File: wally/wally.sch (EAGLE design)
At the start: 103 parts, among them IC1 ESP32-S3-WROOM-1U-N16, IC2 XTLV61048DBVR, IC3 TLV1117LV33DCYR, IC4 DPS310XTSA1, IC5 BMI323, IC6 MCP96L00T-E_MX, IC7 MLX90395KLW-BBA-001-SP, J1 MSD-4-A, J2 QWIIC_RIGHT_ANGLE, J3 QWIIC_RIGHT_ANGLE, J4 S2B-PH-K-S(LF)(SN), J5 USB4105-GF-A, U1 RA-01H

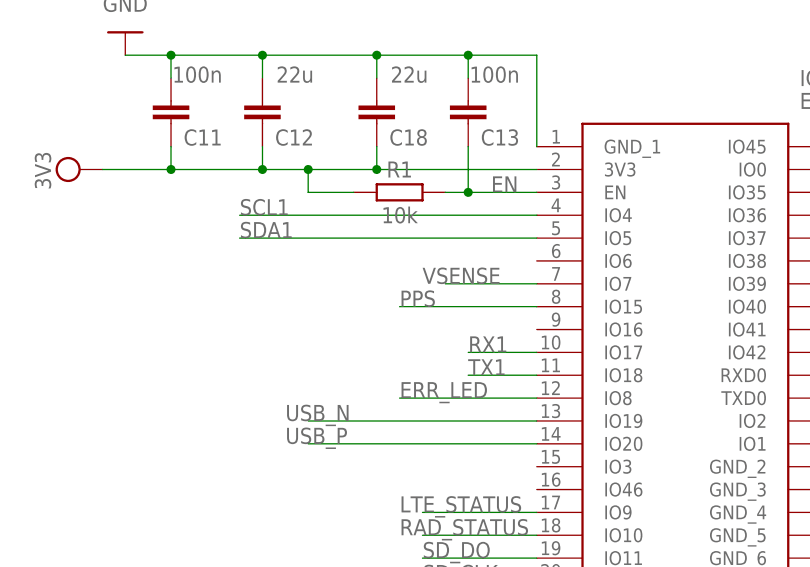
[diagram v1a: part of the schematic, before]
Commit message: add two generic inputs to wally
had two gpio left lol
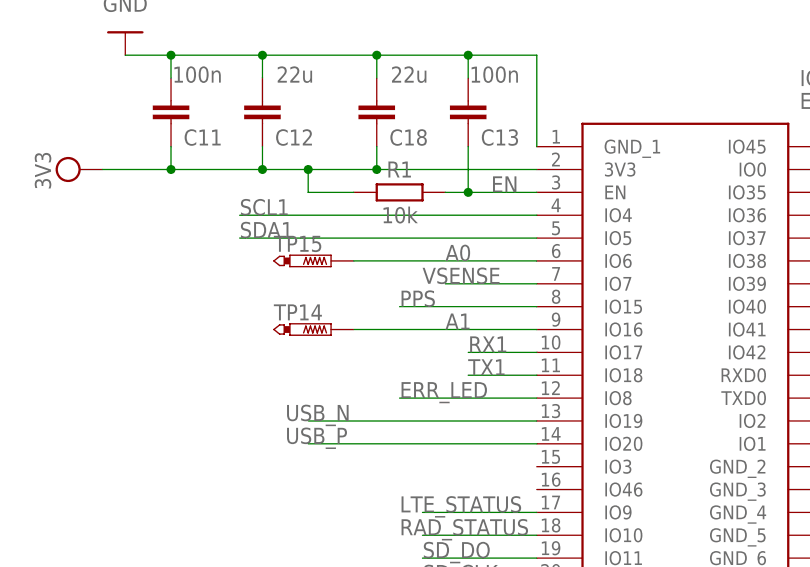
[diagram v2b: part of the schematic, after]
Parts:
- added TP14, TP15: PTR1B2,54, testpad:PTR1B2,54
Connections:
- new net A0: IC1.IO6, TP15.TP
- new net A1: IC1.IO16, TP14.TP
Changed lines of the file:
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@@
 <part name="S1" library="SamacSys_Parts" deviceset="TS-1187A-B-A-B" device="" override_package3d_urn="urn:adsk.eagle:package:44332511/2" override_package_urn="urn:adsk.eagle:footprint:44332512/1"/>
 <part name="S2" library="SamacSys_Parts" deviceset="TS-1187A-B-A-B" device="" override_package3d_urn="urn:adsk.eagle:package:44332514/2" override_package_urn="urn:adsk.eagle:footprint:44332515/1"/>
+<part name="TP14" library="testpad" library_urn="urn:adsk.eagle:library:385" deviceset="PTR1" device="B2,54" package3d_urn="urn:adsk.eagle:package:27948/1"/>
+<part name="TP15" library="testpad" library_urn="urn:adsk.eagle:library:385" deviceset="PTR1" device="B2,54" package3d_urn="urn:adsk.eagle:package:27948/1"/>
 </parts>
 <sheets>
@@
 <attribute name="NAME" x="-130.81" y="15.24" size="1.778" layer="95" align="center-left"/>
 <attribute name="VALUE" x="-130.81" y="12.7" size="1.778" layer="96" align="center-left"/>
+</instance>
+<instance part="TP14" gate="G$1" x="-27.94" y="-22.86" smashed="yes" rot="R270">
+<attribute name="NAME" x="-34.29" y="-21.844" size="1.778" layer="95"/>
+<attribute name="TP_SIGNAL_NAME" x="-30.48" y="-24.13" size="1.778" layer="97" rot="R270"/>
+</instance>
+<instance part="TP15" gate="G$1" x="-27.94" y="-15.24" smashed="yes" rot="R270">
+<attribute name="NAME" x="-34.29" y="-14.224" size="1.778" layer="95"/>
+<attribute name="TP_SIGNAL_NAME" x="-30.48" y="-16.51" size="1.778" layer="97" rot="R270"/>
 </instance>
 </instances>
@@
 </segment>
 </net>
+<net name="A0" class="0">
+<segment>
+<pinref part="IC1" gate="G$1" pin="IO6"/>
+<label x="-15.24" y="-15.24" size="1.778" layer="95"/>
+<pinref part="TP15" gate="G$1" pin="TP"/>
+<wire x1="-25.4" y1="-15.24" x2="-5.08" y2="-15.24" width="0.1524" layer="91"/>
+</segment>
+</net>
+<net name="A1" class="0">
+<segment>
+<pinref part="IC1" gate="G$1" pin="IO16"/>
+<label x="-15.24" y="-22.86" size="1.778" layer="95"/>
+<pinref part="TP14" gate="G$1" pin="TP"/>
+<wire x1="-25.4" y1="-22.86" x2="-5.08" y2="-22.86" width="0.1524" layer="91"/>
+</segment>
+</net>

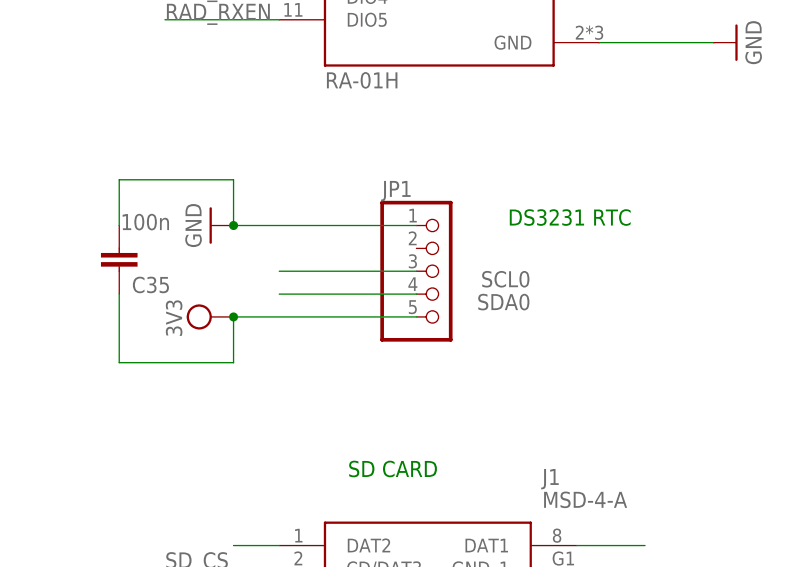
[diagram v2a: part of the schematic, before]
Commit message: move rtc to separate i2c bus
allows all sensors to run at high speed
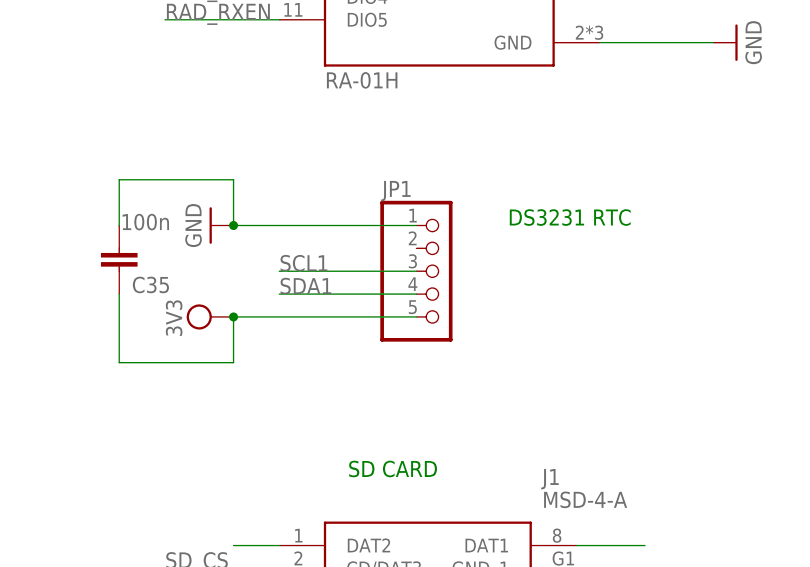
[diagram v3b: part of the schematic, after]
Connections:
- net SCL0: no longer JP1.3
- net SCL1: now also JP1.3
- net SDA0: no longer JP1.4
- net SDA1: now also JP1.4
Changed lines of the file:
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@@
 <net name="SDA0" class="0">
-<segment>
-<pinref part="JP1" gate="A" pin="4"/>
-<wire x1="10.16" y1="-154.94" x2="-5.08" y2="-154.94" width="0.1524" layer="91"/>
-<label x="22.86" y="-154.94" size="1.778" layer="95" rot="R180"/>
-</segment>
 <segment>
 <pinref part="J2" gate="J1" pin="3"/>
@@
 </segment>
 <segment>
-<pinref part="JP1" gate="A" pin="3"/>
-<wire x1="10.16" y1="-152.4" x2="-5.08" y2="-152.4" width="0.1524" layer="91"/>
-<label x="22.86" y="-152.4" size="1.778" layer="95" rot="R180"/>
-</segment>
-<segment>
 <pinref part="R6" gate="G$1" pin="2"/>
 <wire x1="86.36" y1="-30.48" x2="86.36" y2="-38.1" width="0.1524" layer="91"/>
@@
 <label x="-38.1" y="-10.16" size="1.778" layer="95"/>
 </segment>
+<segment>
+<pinref part="JP1" gate="A" pin="3"/>
+<wire x1="10.16" y1="-152.4" x2="-5.08" y2="-152.4" width="0.1524" layer="91"/>
+<label x="-5.08" y="-152.4" size="1.778" layer="95"/>
+</segment>
 </net>
 <net name="SDA1" class="0">
@@
 <label x="-38.1" y="-12.7" size="1.778" layer="95"/>
 </segment>
+<segment>
+<pinref part="JP1" gate="A" pin="4"/>
+<wire x1="10.16" y1="-154.94" x2="-5.08" y2="-154.94" width="0.1524" layer="91"/>
+<label x="-5.08" y="-154.94" size="1.778" layer="95"/>
+</segment>
 </net>

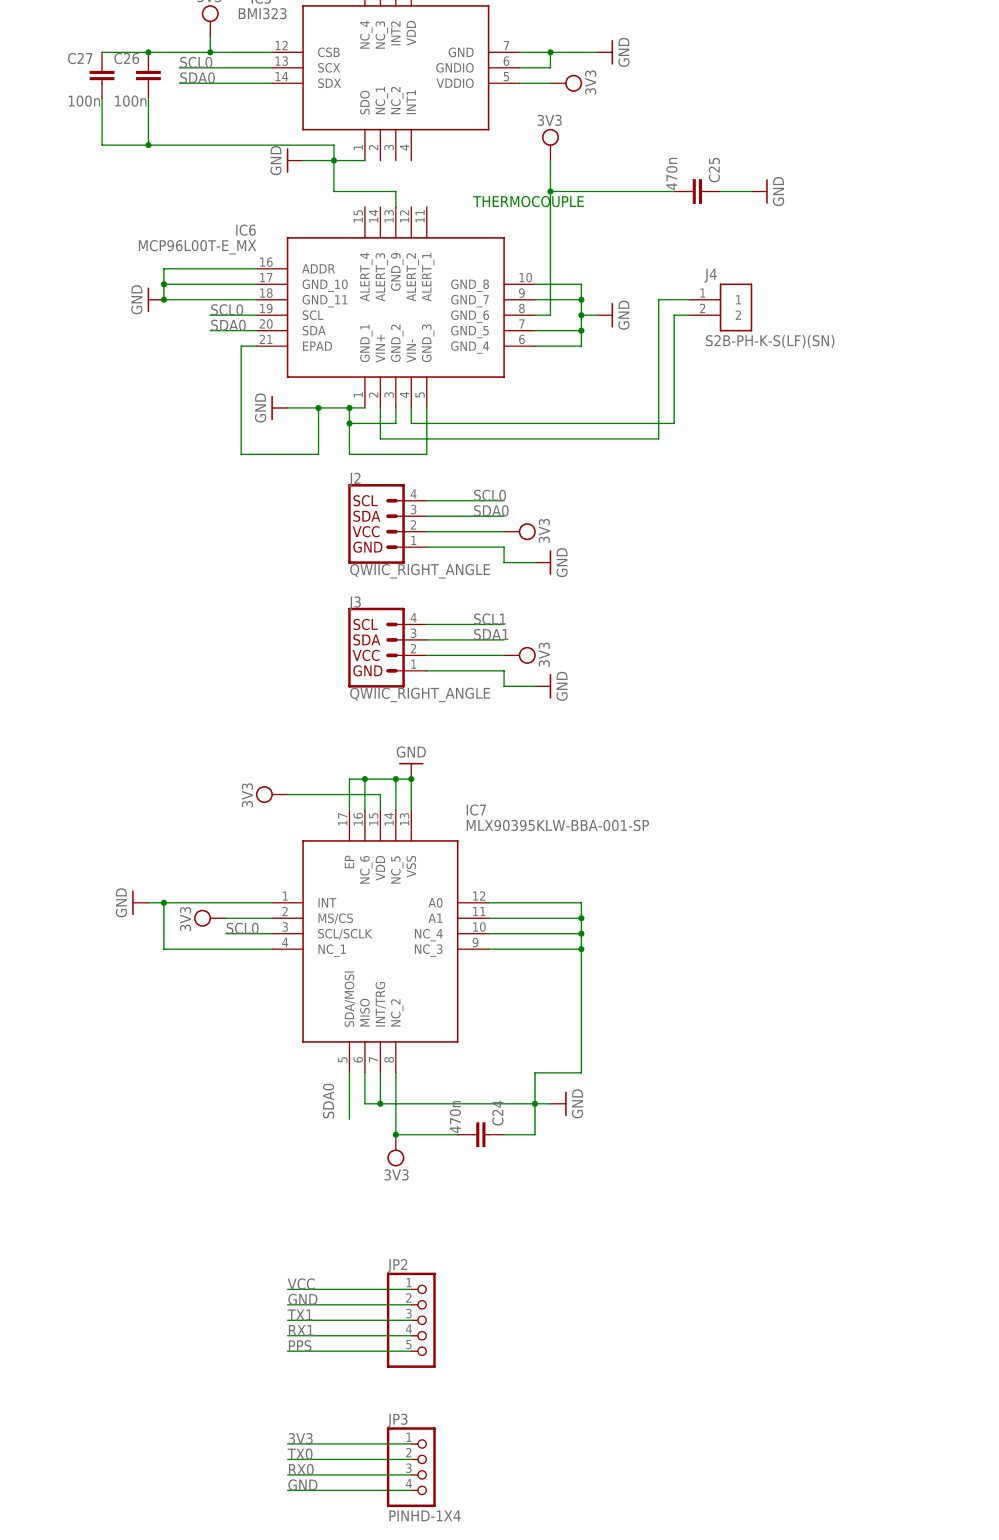
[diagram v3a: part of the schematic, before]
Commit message: remove thermocouple amp
makes more sense to have it externally and connected through i2c
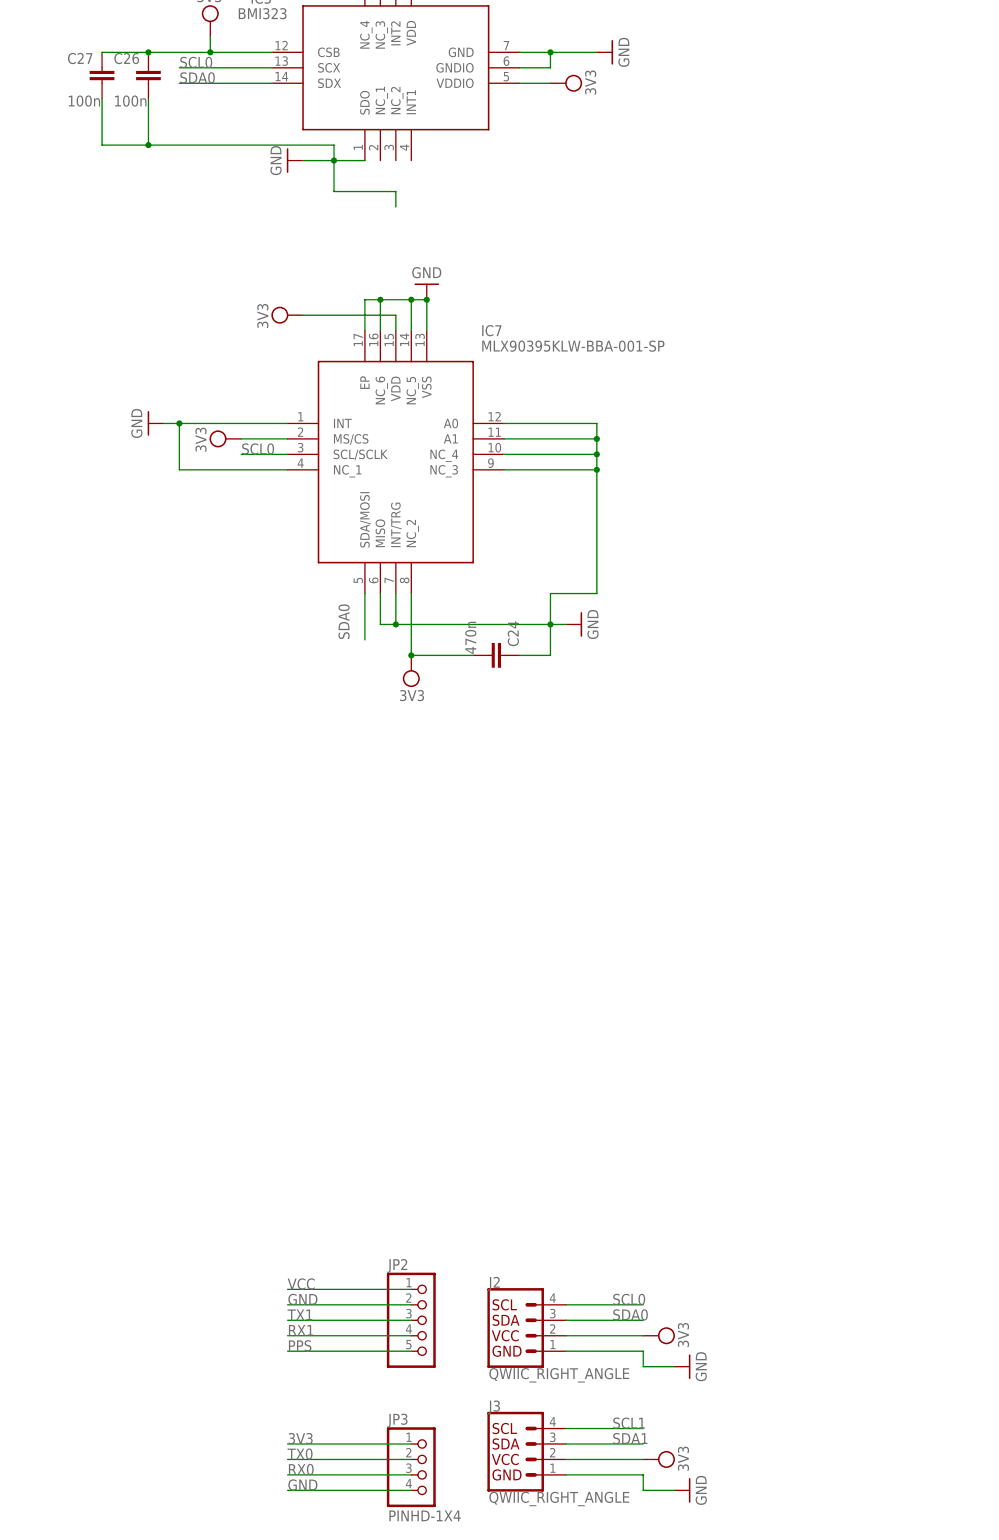
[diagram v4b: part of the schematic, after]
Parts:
- removed C25: 470n, Capacitor:C_CHIP-0603(1608-METRIC)
- removed IC6: MCP96L00T-E_MX, SamacSys_Parts:MCP96L00T-E_MX
- removed J4: S2B-PH-K-S(LF)(SN), Connectors:S2B-PH-K-S(LF)(SN)
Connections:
- removed net N$5: IC6.VIN-, J4.2
- removed net N$6: IC6.VIN+, J4.1
- net 3V3: no longer C25.2, IC6.GND_6
- net GND: no longer C25.1, IC6.ADDR, IC6.EPAD, IC6.GND_1, IC6.GND_10, IC6.GND_11, IC6.GND_2, IC6.GND_3, IC6.GND_4, IC6.GND_5, IC6.GND_7, IC6.GND_8, IC6.GND_9
- net SCL0: no longer IC6.SCL
- net SDA0: no longer IC6.SDA
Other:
- note removed: "THERMOCOUPLE"
- moved on the sheet: C24, IC7, J2, J3

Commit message: use smaller components where available
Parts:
- C1, C10, C11, C13, C14, C15, C16, C17, C19, C23, C26, C27, C28, C29, C3, C35, C8, C9: device Capacitor:C_CHIP-0603(1608-METRIC) -> Capacitor:C_CHIP-0402(1005-METRIC)
- R1, R10, R11, R13, R15, R16, R18, R19, R4, R5, R6, R7, R8, R9: device Resistor:R_CHIP-0603(1608-METRIC) -> Resistor:R_CHIP-0402(1005-METRIC)

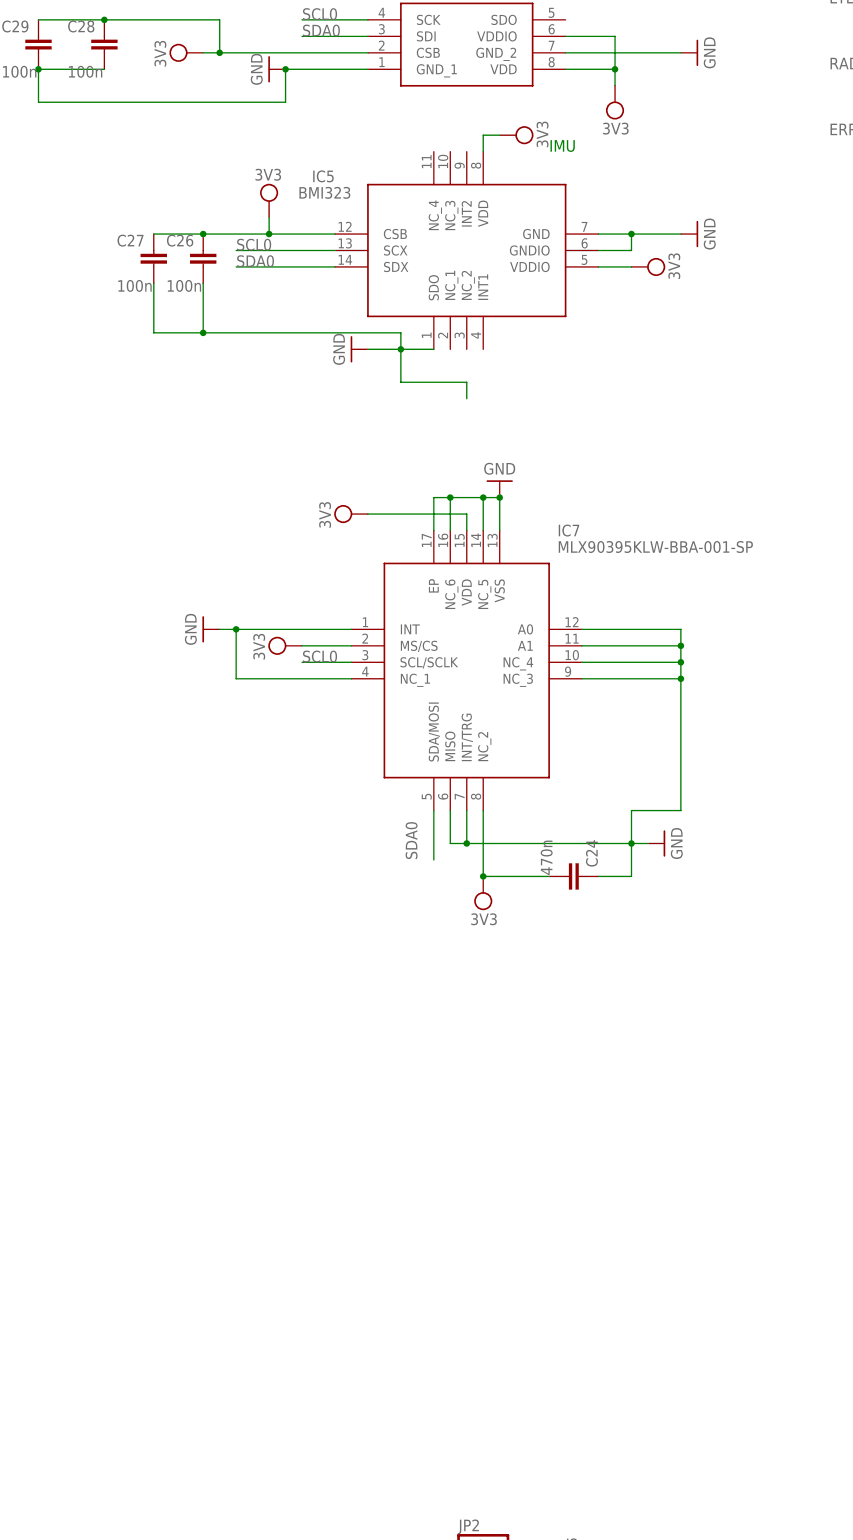
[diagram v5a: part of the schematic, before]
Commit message: change to lsm6dsv imu
+- 32g and integrated sensor fusion
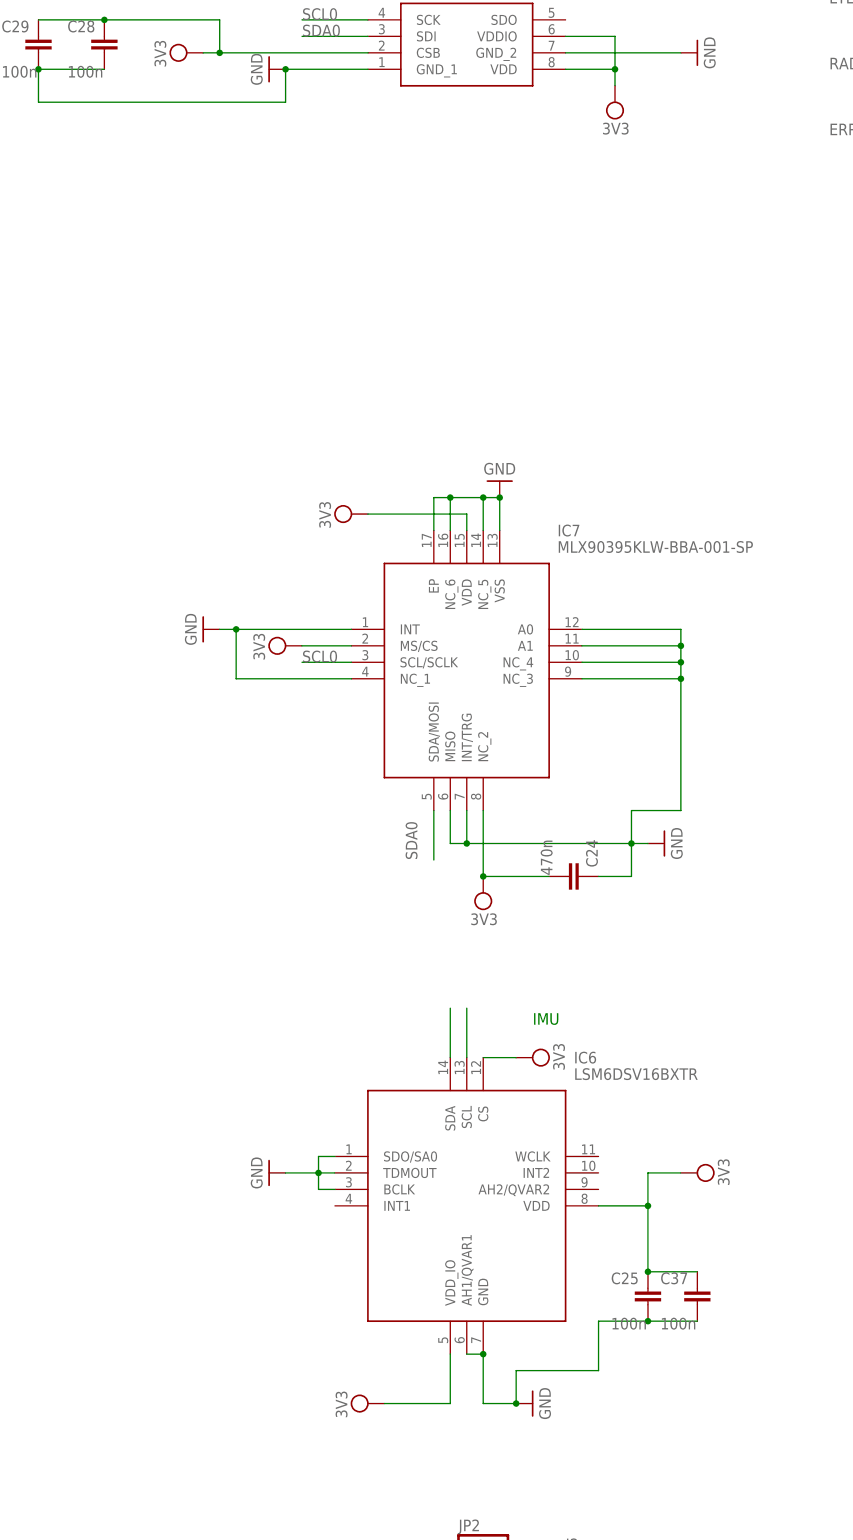
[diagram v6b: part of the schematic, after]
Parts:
- removed C26, C27: 100n, Capacitor:C_CHIP-0402(1005-METRIC)
- removed IC5: BMI323, SamacSys_Parts:BMI323
- added C25, C37: 100n, Capacitor:C_CHIP-0402(1005-METRIC)
- added IC6: LSM6DSV16BXTR, SamacSys_Parts:LSM6DSV16BXTR
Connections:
- new net N$5: IC6.SDA
- new net N$6: IC6.SCL
- net 3V3: now also C25.1, C37.1, IC6.CS, IC6.VDD, IC6.VDD_IO; no longer C26.1, C27.1, IC5.CSB, IC5.VDD, IC5.VDDIO
- net GND: now also C25.2, C37.2, IC6.AH1/QVAR1, IC6.BCLK, IC6.GND, IC6.SDO/SA0, IC6.TDMOUT; no longer C26.2, C27.2, IC5.GND, IC5.GNDIO, IC5.SDO
- net SCL0: no longer IC5.SCX
- net SDA0: no longer IC5.SDX
